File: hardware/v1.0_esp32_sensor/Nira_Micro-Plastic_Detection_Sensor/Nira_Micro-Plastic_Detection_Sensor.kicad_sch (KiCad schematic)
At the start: 5 parts, among them U1 PC_FDC1004, U2 DEVKIT_V1_ESP32-WROOM-32

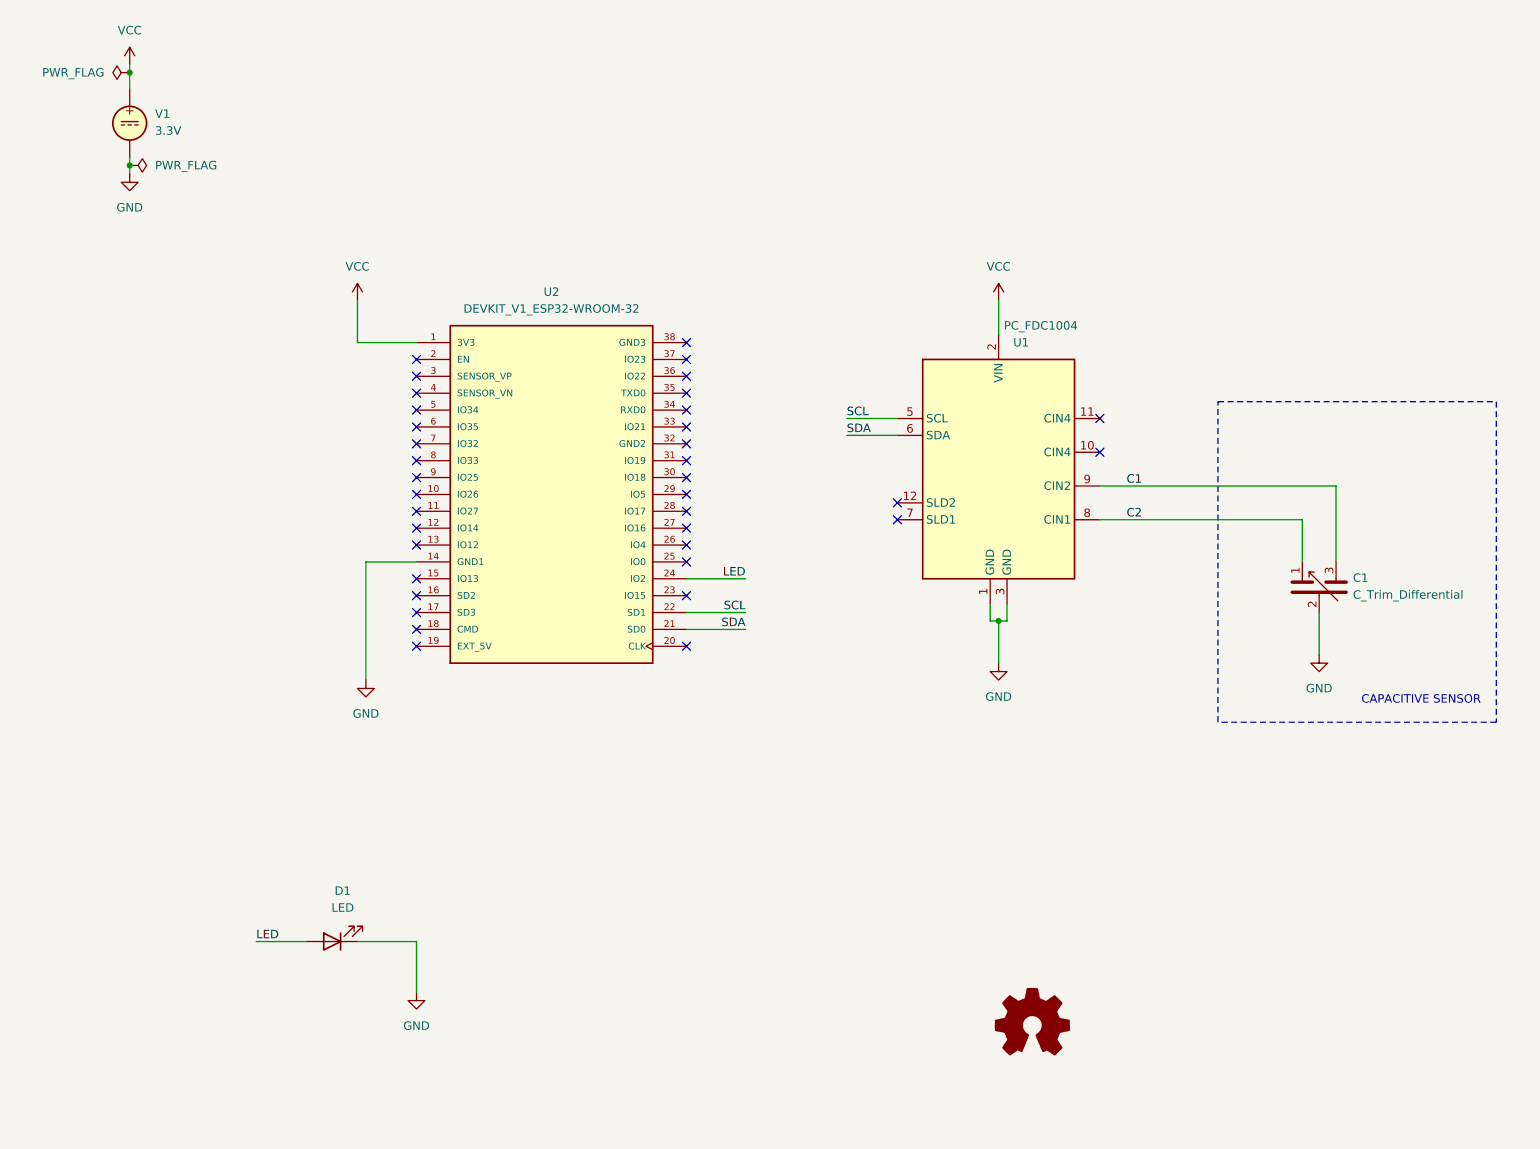
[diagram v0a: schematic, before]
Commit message: LED protection resistor added
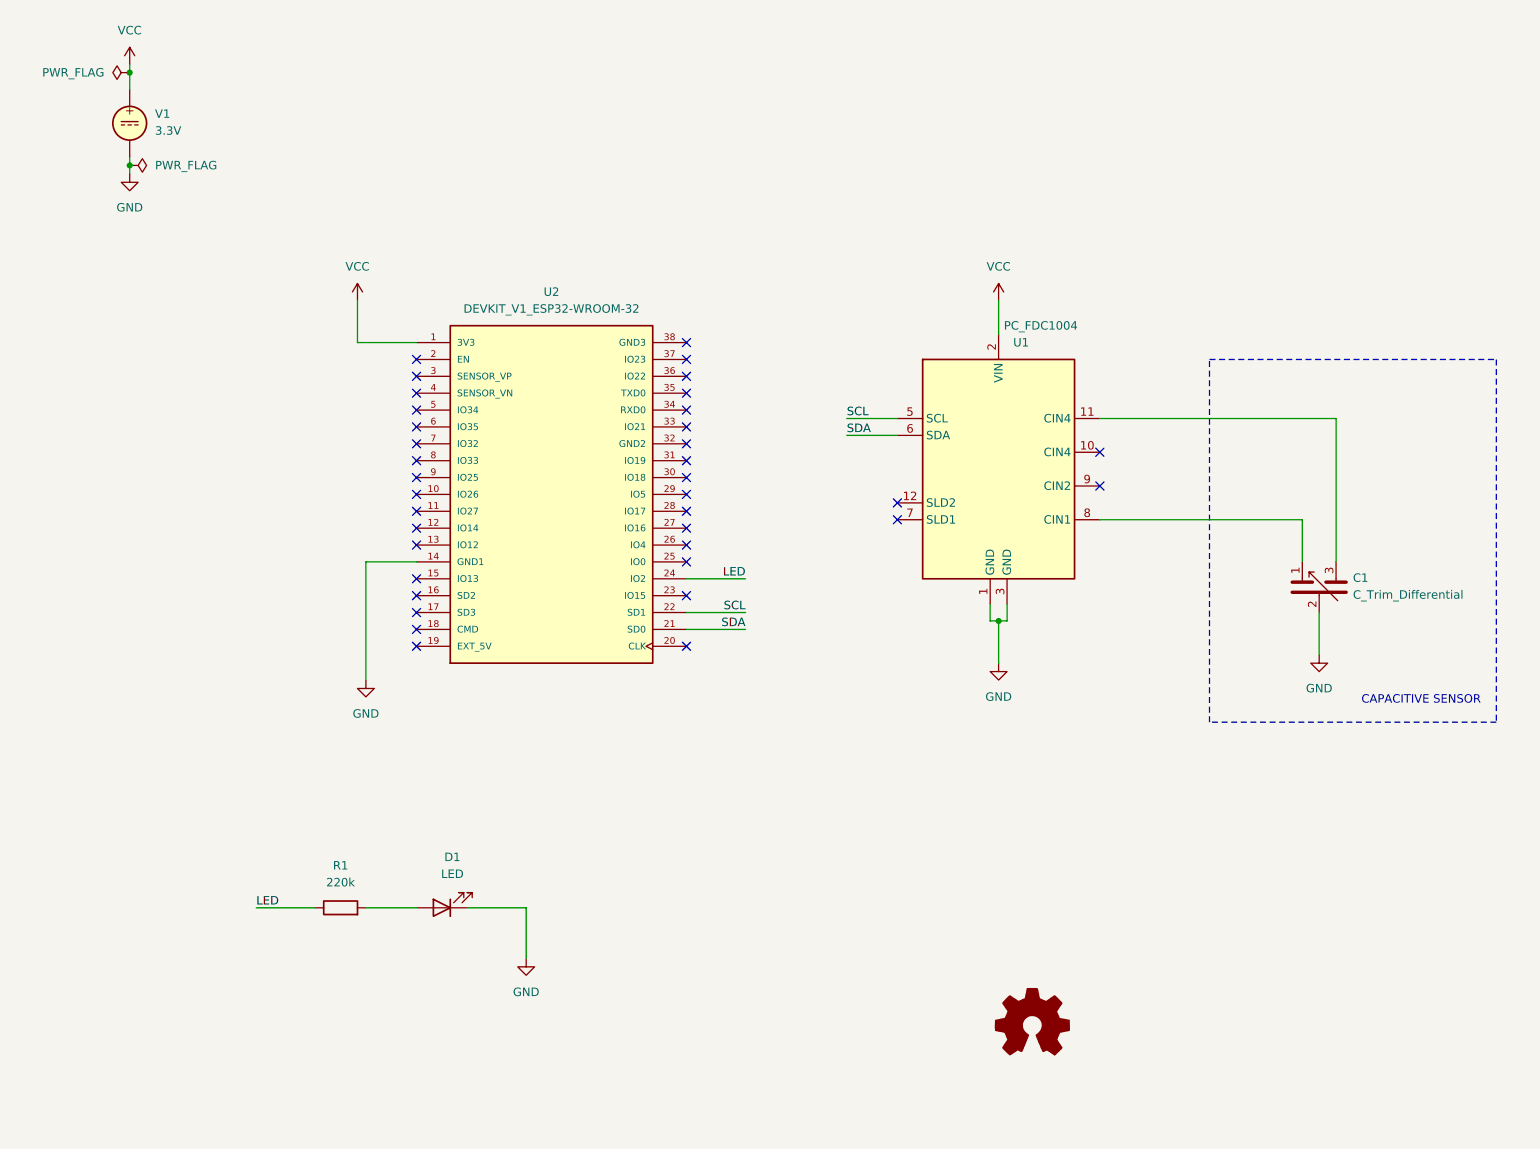
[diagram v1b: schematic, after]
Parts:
- added R1: 220k, symbol Device:R
- D1: footprint (none) -> LED_THT:LED_D3.0mm_Clear
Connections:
- net LED: now also R1.1; no longer D1.2 (A)
- net at U1.11 (CIN4): now also C1.3
- net C1: no longer names the net of U1.9 (CIN2)
- net C1: no longer C1.3
- net C2: no longer names the net of C1.1, U1.8 (CIN1)
- new net: D1.2 (A), R1.2
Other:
- moved on the sheet: D1
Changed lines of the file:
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@@
   (no_connect (at 76.2 73.66))
   (no_connect (at 116.84 81.28))
-  (no_connect (at 179.07 82.55))
+  (no_connect (at 179.07 92.71))
   (no_connect (at 116.84 73.66))
   (no_connect (at 116.84 88.9))
@@
     (stroke (width 0) (type default))
   )
-  (wire (pts (xy 179.07 92.71) (xy 214.63 92.71))
-    (stroke (width 0) (type default))
-  )
-  (wire (pts (xy 52.07 161.29) (xy 59.69 161.29))
+  (wire (pts (xy 52.07 156.21) (xy 60.96 156.21))
+    (stroke (width 0) (type default))
+  )
+  (wire (pts (xy 68.58 156.21) (xy 76.2 156.21))
     (stroke (width 0) (type default))
   )
@@
     (stroke (width 0) (type default))
   )
-  (wire (pts (xy 76.2 161.29) (xy 76.2 168.91))
+  (wire (pts (xy 92.71 156.21) (xy 92.71 163.83))
     (stroke (width 0) (type default))
   )
@@
     (stroke (width 0) (type default))
   )
-  (wire (pts (xy 214.63 92.71) (xy 214.63 104.14))
+  (wire (pts (xy 179.07 82.55) (xy 214.63 82.55))
+    (stroke (width 0) (type default))
+  )
+  (wire (pts (xy 214.63 82.55) (xy 214.63 104.14))
     (stroke (width 0) (type default))
   )
@@
     (stroke (width 0) (type default))
   )
-  (wire (pts (xy 67.31 161.29) (xy 76.2 161.29))
+  (wire (pts (xy 83.82 156.21) (xy 92.71 156.21))
     (stroke (width 0) (type default))
   )
@@
     (stroke (width 0) (type default))
   )
-  (rectangle (start 196.85 80.01) (end 238.76 128.27)
+  (rectangle (start 195.58 73.66) (end 238.76 128.27)
     (stroke (width 0) (type dash))
     (fill (type none))
@@
     (effects (font (size 1.27 1.27)) (justify left bottom))
   )
-  (label "C2" (at 185.42 97.79 180) (fields_autoplaced)
-    (effects (font (size 1.27 1.27)) (justify right bottom))
-  )
   (label "LED" (at 125.73 106.68 180) (fields_autoplaced)
     (effects (font (size 1.27 1.27)) (justify right bottom))
   )
-  (label "LED" (at 52.07 161.29 0) (fields_autoplaced)
+  (label "LED" (at 52.07 156.21 0) (fields_autoplaced)
     (effects (font (size 1.27 1.27)) (justify left bottom))
   )
   (label "SCL" (at 125.73 111.76 180) (fields_autoplaced)
-    (effects (font (size 1.27 1.27)) (justify right bottom))
-  )
-  (label "C1" (at 185.42 92.71 180) (fields_autoplaced)
     (effects (font (size 1.27 1.27)) (justify right bottom))
   )
@@
     )
   )
-  (symbol (lib_id "Device:LED") (at 63.5 161.29 180) (unit 1)
-    (in_bom yes) (on_board yes) (dnp no) (fields_autoplaced)
-    (property "Reference" "D1" (at 65.0875 153.67 0)
-      (effects (font (size 1.27 1.27)))
-    )
-    (property "Value" "LED" (at 65.0875 156.21 0)
-      (effects (font (size 1.27 1.27)))
-    )
-    (property "Footprint" "" (at 63.5 161.29 0)
-      (effects (font (size 1.27 1.27)) hide)
-    )
-    (property "Datasheet" "~" (at 63.5 161.29 0)
+  (symbol (lib_id "Device:LED") (at 80.01 156.21 180) (unit 1)
+    (in_bom yes) (on_board yes) (dnp no) (fields_autoplaced)
+    (property "Reference" "D1" (at 81.5975 148.59 0)
+      (effects (font (size 1.27 1.27)))
+    )
+    (property "Value" "LED" (at 81.5975 151.13 0)
+      (effects (font (size 1.27 1.27)))
+    )
+    (property "Footprint" "LED_THT:LED_D3.0mm_Clear" (at 80.01 156.21 0)
+      (effects (font (size 1.27 1.27)) hide)
+    )
+    (property "Datasheet" "~" (at 80.01 156.21 0)
       (effects (font (size 1.27 1.27)) hide)
     )
@@
         (path "/3f60aafb-dfb1-4dd9-9864-0936d5873a60"
           (reference "D1") (unit 1)
+        )
+      )
+    )
+  )
+  (symbol (lib_id "Device:R") (at 64.77 156.21 90) (unit 1)
+    (in_bom yes) (on_board yes) (dnp no) (fields_autoplaced)
+    (property "Reference" "R1" (at 64.77 149.86 90)
+      (effects (font (size 1.27 1.27)))
+    )
+    (property "Value" "220k" (at 64.77 152.4 90)
+      (effects (font (size 1.27 1.27)))
+    )
+    (property "Footprint" "" (at 64.77 157.988 90)
+      (effects (font (size 1.27 1.27)) hide)
+    )
+    (property "Datasheet" "~" (at 64.77 156.21 0)
+      (effects (font (size 1.27 1.27)) hide)
+    )
+    (pin "2")
+    (pin "1")
+    (instances
+      (project "Nira_Micro-Plastic_Detection_Sensor"
+        (path "/3f60aafb-dfb1-4dd9-9864-0936d5873a60"
+          (reference "R1") (unit 1)
         )
       )
@@
     )
   )
-  (symbol (lib_name "GND_1") (lib_id "power:GND") (at 76.2 168.91 0) (unit 1)
-    (in_bom yes) (on_board yes) (dnp no) (fields_autoplaced)
-    (property "Reference" "#PWR05" (at 76.2 175.26 0)
-      (effects (font (size 1.27 1.27)) hide)
-    )
-    (property "Value" "GND" (at 76.2 173.99 0)
-      (effects (font (size 1.27 1.27)))
-    )
-    (property "Footprint" "" (at 76.2 168.91 0)
-      (effects (font (size 1.27 1.27)) hide)
-    )
-    (property "Datasheet" "" (at 76.2 168.91 0)
-      (effects (font (size 1.27 1.27)) hide)
-    )
+  (symbol (lib_name "GND_1") (lib_id "power:GND") (at 92.71 163.83 0) (unit 1)
+    (in_bom yes) (on_board yes) (dnp no) (fields_autoplaced)
+    (property "Reference" "#PWR05" (at 92.71 170.18 0)
+      (effects (font (size 1.27 1.27)) hide)
+    )
+    (property "Value" "GND" (at 92.71 168.91 0)
+      (effects (font (size 1.27 1.27)))
+    )
+    (property "Footprint" "" (at 92.71 163.83 0)
+      (effects (font (size 1.27 1.27)) hide)
+    )
+    (property "Datasheet" "" (at 92.71 163.83 0)
+      (effects (font (size 1.27 1.27)) hide)
+    )

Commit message: test data imported and visulaised using GUN Octave
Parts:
- added M1: Motor_DC, symbol Motor:Motor_DC
- added V2: 5.0V, symbol Simulation_SPICE:VDC
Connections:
- net GND: now also M1.2 (-), V2.2
- new net VDC: M1.1 (+), V2.1
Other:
- note added: "ESP32 DEVKIT V1"
- note added: "PROTOCENTRAL FDC1004 MODULE"
- note added: "WATER PUMP DC"
- moved on the sheet: D1, R1, V1

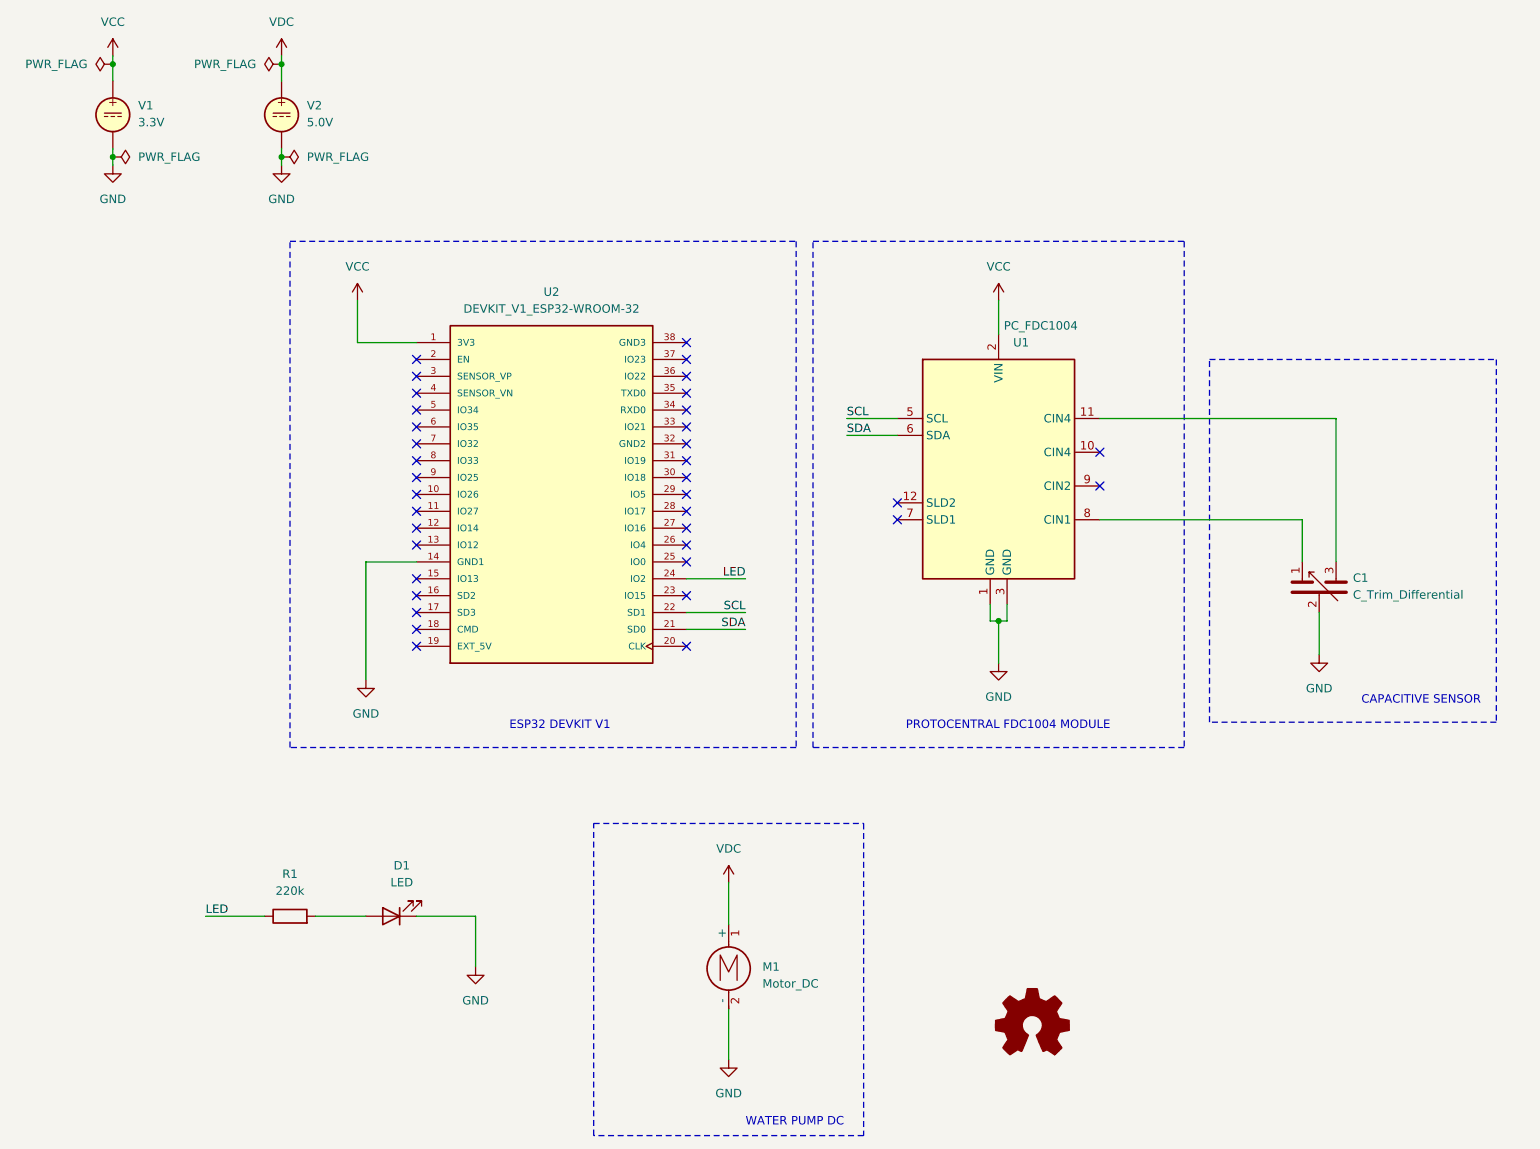
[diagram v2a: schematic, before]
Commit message: docs: complete OSHW documentation v1.0
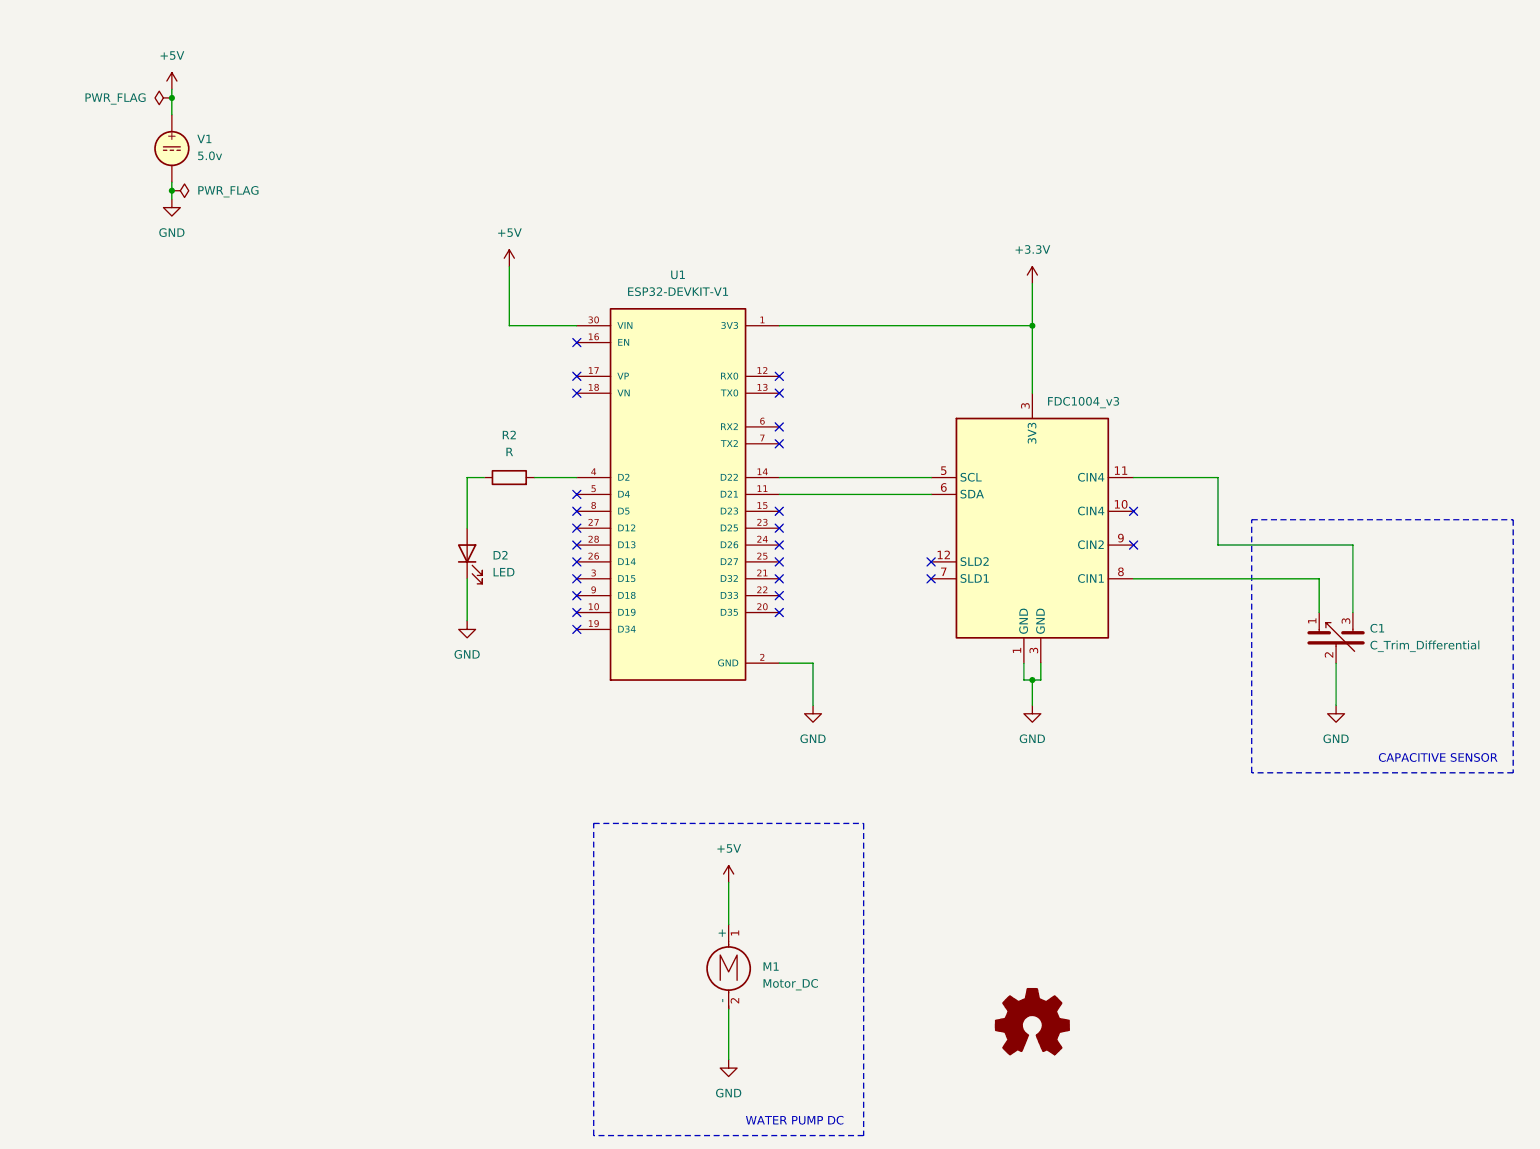
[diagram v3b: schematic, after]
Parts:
- removed D1: LED, LED_THT:LED_D3.0mm_Clear, symbol Device:LED
- removed R1: 220k, symbol Device:R
- removed U1: PC_FDC1004, symbol Nira_Capacitive_sence:PC_FDC1004
- removed U2: DEVKIT_V1_ESP32-WROOM-32, DEVKIT_V1_ESP32-WROOM-32:MODULE_DEVKIT_V1_ESP32-WROOM-32, symbol Nira_Capacitive_sence:DEVKIT_V1_ESP32-WROOM-32
- removed V2: 5.0V, symbol Simulation_SPICE:VDC
- added D2: LED, symbol Device:LED
- added FDC1004_v3: ~, symbol New_Library:PC_FDC_1004_V3
- added R2: R, symbol Device:R
- added U1: ESP32-DEVKIT-V1, ESP32-DEVKIT-V1:MODULE_ESP32_DEVKIT_V1, symbol ESP32-DEVKIT-V1:ESP32-DEVKIT-V1
- V1: value 3.3V -> 5.0v
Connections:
- net VDC is gone; now on net +5V: M1.1 (+)
- net GND: now also D2.1 (K), FDC1004_v3.1 (GND), FDC1004_v3.3 (GND), U1.2 (GND), U1.29 (GND)
- net at C1.1: now also FDC1004_v3.8 (CIN1)
- net at C1.3: now also FDC1004_v3.11 (CIN4)
- net VCC renamed +5V
- net +5V: now also U1.30 (VIN)
- new net: D2.2 (A), R2.1
- new net: R2.2, U1.4 (D2)
- new net: FDC1004_v3.5 (SCL), U1.14 (D22)
- new net: FDC1004_v3.6 (SDA), U1.11 (D21)
- new net +3.3V: FDC1004_v3.3 (GND), U1.1 (3V3)
- no-connect marks 37 -> 27
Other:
- note removed: "ESP32 DEVKIT V1"
- note removed: "PROTOCENTRAL FDC1004 MODULE"
- moved on the sheet: V1
